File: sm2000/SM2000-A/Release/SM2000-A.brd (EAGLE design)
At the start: 160 x 160 mm, 456 parts, among them CN1 HDR100-3, CN2 ST-3509, CN3 HDR100-3, CN4 JS-MU3-002, CN5 DS-0518, CN6 ST-3509, CN7 ST-3509, J1 JMP-2PIN, J10 JMPR-2X2, J11 JMPR-2X2, J12 JMPR-2X2, J13 JMPR-2X2, J14 JMPR-2X2, J2 HDR100-7, J3 JMP-2PIN, J4 CONN-BOOM-XH-2A, J5 JMP-2PIN, J6 JMPR-2X2, J7 JMPR-2X2, J8 JMPR-2X2, J9 JMPR-2X2, P6 TPAD50, P7 TPAD50, P8 TPAD50, P9 TPAD50, Q1 MMBT3904, Q10 MMBT3904, Q11 BFR92, Q12 BFQ19, Q13 RD01MUS2, Q14 MMBT3904, Q15 MMBT3904, Q16 MMBT3904, Q17 MMBT3906, Q2 STR2P3LLH6, Q3 MMBT3904, Q4 STR2P3LLH6, Q5 MMBT3904, Q6 MMBT3904, Q7 MMBT3904, Q8 MMBT3904, Q9 MMBT3904, SW1 TS-02B, SW2 SW-LC2259, SW3 TS-026, SW4 TS-026, SW5 SW-LC2259EENP, U1 STM32F405VGT6, U10 LM386M-1, U11 ADE-1, U12 PGA-103+, U13 LMV341, U14 SI5351A, U15 SI570, U16 SA612A, U2 STMPS2141, U3 EMIF02-USB03F2, U4 DNL, U5 L78M09, U6 LD1117AS-33, U7 LMV341, U8 LD1117AS-33, U9 TPS54329E, X1 BU-SMA-H

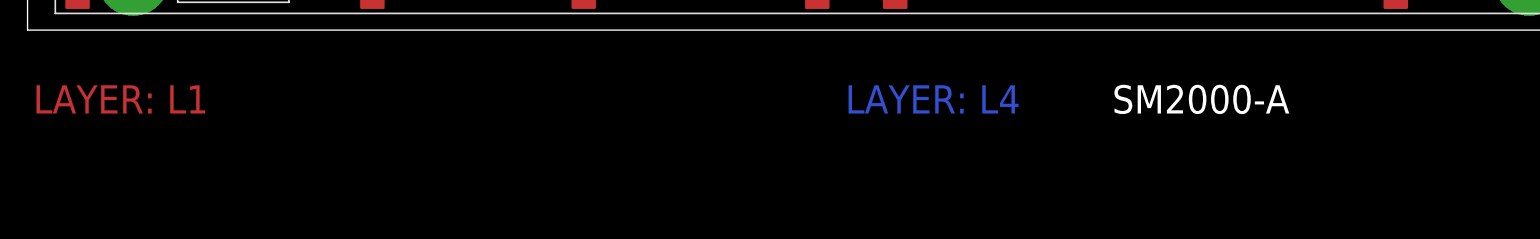
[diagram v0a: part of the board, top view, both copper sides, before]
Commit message: SM2000-A Folders should now be current. RGB
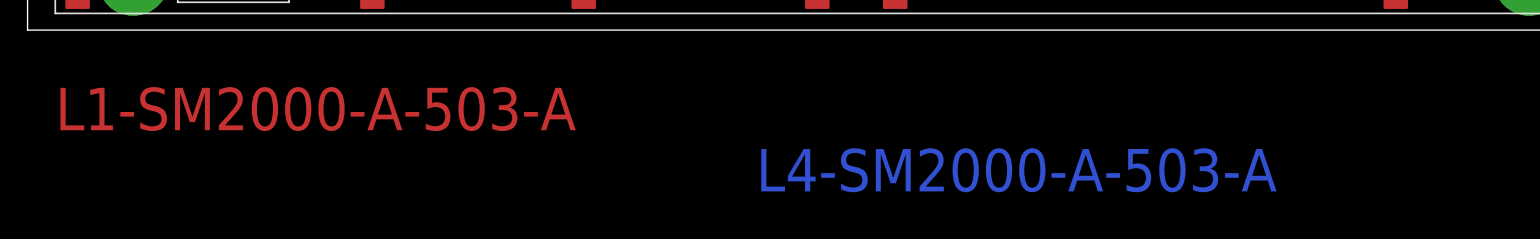
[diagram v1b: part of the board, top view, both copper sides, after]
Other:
- board text added: "L1-SM2000-A-503-A"
- board text added: "L2-SM2000-A-503-A"
- board text added: "L3-SM2000-A-503-A"
- board text added: "L4-SM2000-A-503-A"
- board text removed: ">DRAWING_NAME"
- board text removed: ">LAST_DATE_TIME"
- board text removed: "LAYER: L1"
- board text removed: "LAYER: L2"
- board text removed: "LAYER: L3"
- board text removed: "LAYER: L4"
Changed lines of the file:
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@@
 <grid distance="0.5" unitdist="mm" unit="mm" style="dots" multiple="1" display="yes" altdistance="0.1" altunitdist="mm" altunit="mm"/>
 <layers>
-<layer number="1" name="L1-TOP" color="4" fill="1" visible="yes" active="yes"/>
-<layer number="2" name="L2-GND" color="2" fill="1" visible="yes" active="yes"/>
+<layer number="1" name="L1-TOP" color="4" fill="1" visible="no" active="yes"/>
+<layer number="2" name="L2-GND" color="2" fill="1" visible="no" active="yes"/>
 <layer number="3" name="Route3" color="4" fill="3" visible="no" active="yes"/>
 <layer number="4" name="Route4" color="1" fill="4" visible="no" active="no"/>
@@
 <layer number="13" name="Route13" color="4" fill="5" visible="no" active="no"/>
 <layer number="14" name="Route14" color="1" fill="6" visible="no" active="no"/>
-<layer number="15" name="L3-VDD" color="3" fill="1" visible="yes" active="yes"/>
+<layer number="15" name="L3-VDD" color="3" fill="1" visible="no" active="yes"/>
 <layer number="16" name="L4-BOTTOM" color="1" fill="1" visible="yes" active="yes"/>
-<layer number="17" name="Pads" color="2" fill="1" visible="no" active="yes"/>
-<layer number="18" name="Vias" color="2" fill="1" visible="no" active="yes"/>
+<layer number="17" name="Pads" color="2" fill="1" visible="yes" active="yes"/>
+<layer number="18" name="Vias" color="2" fill="1" visible="yes" active="yes"/>
 <layer number="19" name="Unrouted" color="6" fill="1" visible="no" active="yes"/>
 <layer number="20" name="Dimension" color="15" fill="1" visible="yes" active="yes"/>
-<layer number="21" name="tPlace" color="15" fill="1" visible="no" active="yes"/>
-<layer number="22" name="bPlace" color="7" fill="1" visible="no" active="yes"/>
+<layer number="21" name="tPlace" color="15" fill="1" visible="yes" active="yes"/>
+<layer number="22" name="bPlace" color="7" fill="1" visible="yes" active="yes"/>
 <layer number="23" name="tOrigins" color="15" fill="1" visible="no" active="yes"/>
 <layer number="24" name="bOrigins" color="15" fill="1" visible="no" active="yes"/>
-<layer number="25" name="tNames" color="7" fill="1" visible="no" active="yes"/>
-<layer number="26" name="bNames" color="7" fill="1" visible="no" active="yes"/>
+<layer number="25" name="tNames" color="7" fill="1" visible="yes" active="yes"/>
+<layer number="26" name="bNames" color="7" fill="1" visible="yes" active="yes"/>
 <layer number="27" name="tValues" color="7" fill="1" visible="no" active="yes"/>
 <layer number="28" name="bValues" color="7" fill="1" visible="no" active="yes"/>
@@
 <wire x1="101" y1="99" x2="131.5" y2="99" width="0.15" layer="21"/>
 <wire x1="131.5" y1="99" x2="131.5" y2="121" width="0.15" layer="21"/>
-<text x="0.5" y="-7.5" size="2.54" layer="1" font="vector" ratio="10">LAYER: L1</text>
-<text x="24.5" y="-7.5" size="2.54" layer="2" font="vector" ratio="10">LAYER: L2</text>
-<text x="49" y="-7.5" size="2.54" layer="15" font="vector" ratio="10">LAYER: L3</text>
-<text x="73.5" y="-7.5" size="2.54" layer="16" font="vector" ratio="10" rot="SR0">LAYER: L4</text>
+<text x="2.5" y="-9" size="3.81" layer="1" font="vector" ratio="10">L1-SM2000-A-503-A</text>
+<text x="65.5" y="-9" size="3.81" layer="2" font="vector" ratio="10">L2-SM2000-A-503-A</text>
+<text x="3" y="-14.5" size="3.81" layer="15" font="vector" ratio="10">L3-SM2000-A-503-A</text>
+<text x="65.5" y="-14.5" size="3.81" layer="16" font="vector" ratio="10" rot="SR0">L4-SM2000-A-503-A</text>
 <text x="155" y="120.5" size="1.27" layer="21" ratio="10" rot="SR270">BASEBAND
 AMP</text>
@@
 <wire x1="160.5" y1="-0.5" x2="155" y2="-0.5" width="1" layer="206"/>
 <wire x1="160.5" y1="-0.5" x2="160.5" y2="5" width="1" layer="206"/>
-<text x="120.5" y="-7.5" size="2.54" layer="20" font="vector" ratio="10">&gt;LAST_DATE_TIME</text>
-<text x="97.5" y="-7.5" size="2.54" layer="20" font="vector" ratio="10">&gt;DRAWING_NAME</text>
-<text x="97.5" y="-7.5" size="2.54" layer="206" font="vector" ratio="10">&gt;DRAWING_NAME</text>
-<text x="120.5" y="-7.5" size="2.54" layer="206" font="vector" ratio="10">&gt;LAST_DATE_TIME</text>
-<text x="97.5" y="-7.5" size="2.54" layer="1" font="vector" ratio="10">&gt;DRAWING_NAME</text>
-<text x="97.5" y="-7.5" size="2.54" layer="2" font="vector" ratio="10">&gt;DRAWING_NAME</text>
-<text x="97.5" y="-7.5" size="2.54" layer="15" font="vector" ratio="10">&gt;DRAWING_NAME</text>
-<text x="97.5" y="-7.5" size="2.54" layer="16" font="vector" ratio="10">&gt;DRAWING_NAME</text>
-<text x="120.5" y="-7.5" size="2.54" layer="1" font="vector" ratio="10">&gt;LAST_DATE_TIME</text>
-<text x="120.5" y="-7.5" size="2.54" layer="2" font="vector" ratio="10">&gt;LAST_DATE_TIME</text>
-<text x="120.5" y="-7.5" size="2.54" layer="15" font="vector" ratio="10">&gt;LAST_DATE_TIME</text>
-<text x="120.5" y="-7.5" size="2.54" layer="16" font="vector" ratio="10">&gt;LAST_DATE_TIME</text>
 </plain>
 <attributes>
